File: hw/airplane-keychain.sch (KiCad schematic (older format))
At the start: 11 parts, among them IC1 ATTINY85-P, SW1 SW_PUSH, SW2 SPST

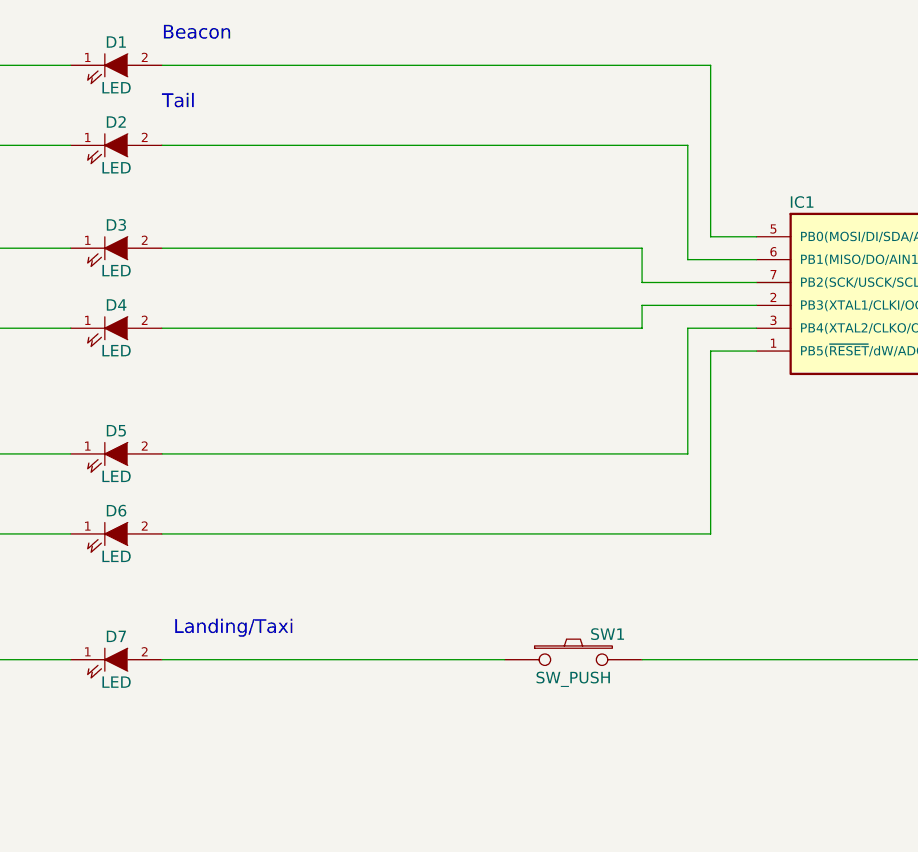
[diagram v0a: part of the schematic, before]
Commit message: added current limiting resistors
swapped out battery connector
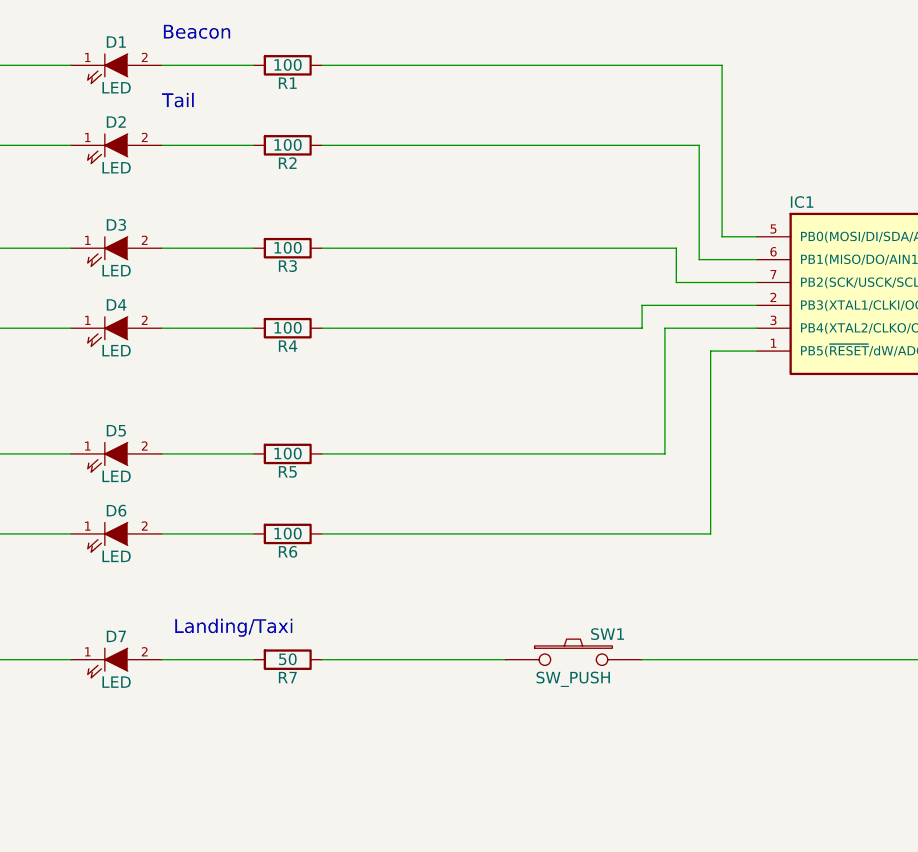
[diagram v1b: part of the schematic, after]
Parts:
- added R1, R2, R3, R4, R5, R6: 100, Resistors_ThroughHole:R_Axial_DIN0207_L6.3mm_D2.5mm_P2.54mm_Vertical, symbol R
- added R7: 50, Resistors_ThroughHole:R_Axial_DIN0207_L6.3mm_D2.5mm_P2.54mm_Vertical, symbol R
- BT1: footprint Battery_Holders:Keystone_2468_2xAAA -> Connectors_JST:JST_PH_B2B-PH-K_02x2.00mm_Straight
- SW1: footprint Buttons_Switches_ThroughHole:SW_PUSH-12mm -> Buttons_Switches_ThroughHole:SW_PUSH_SMALL
- SW2: footprint Buttons_Switches_ThroughHole:SW_DIP_x1_W7.62mm_Slide -> Buttons_Switches_ThroughHole:SW_Micro_SPST
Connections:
- net at D1.2 (A): now also R1.2; no longer IC1.5 (PB0(MOSI/DI/SDA/AIN0/OC0A/OC1A/AREF/PCINT0))
- net at D2.2 (A): now also R2.2; no longer IC1.6 (PB1(MISO/DO/AIN1/OC0B/OC1A/PCINT1))
- net at D3.2 (A): now also R3.2; no longer IC1.7 (PB2(SCK/USCK/SCL/T0/INT0/ADC1/PCINT2))
- net at D4.2 (A): now also R4.2; no longer IC1.2 (PB3(XTAL1/CLKI/OC1B/ADC3/PCINT3))
- net at D5.2 (A): now also R5.2; no longer IC1.3 (PB4(XTAL2/CLKO/OC1B/ADC2/PCINT4))
- net at D6.2 (A): now also R6.2; no longer IC1.1 (PB5(~RESET~/dW/ADC0/PCINT5))
- net at D7.2 (A): now also R7.2; no longer SW1.1
- new net: R7.1, SW1.1
- new net: IC1.1 (PB5(~RESET~/dW/ADC0/PCINT5)), R6.1
- new net: IC1.2 (PB3(XTAL1/CLKI/OC1B/ADC3/PCINT3)), R4.1
- new net: IC1.3 (PB4(XTAL2/CLKO/OC1B/ADC2/PCINT4)), R5.1
- new net: IC1.5 (PB0(MOSI/DI/SDA/AIN0/OC0A/OC1A/AREF/PCINT0)), R1.1
- new net: IC1.6 (PB1(MISO/DO/AIN1/OC0B/OC1A/PCINT1)), R2.1
- new net: IC1.7 (PB2(SCK/USCK/SCL/T0/INT0/ADC1/PCINT2)), R3.1
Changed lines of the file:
@@
 F 0 "SW1" H 3950 3860 50  0000 C CNN
 F 1 "SW_PUSH" H 3800 3670 50  0000 C CNN
-F 2 "Buttons_Switches_ThroughHole:SW_PUSH-12mm" H 3800 3750 50  0001 C CNN
+F 2 "Buttons_Switches_ThroughHole:SW_PUSH_SMALL" H 3800 3750 50  0001 C CNN
 F 3 "" H 3800 3750 50  0000 C CNN
 	1    3800 3750
@@
 F 0 "BT1" H 8400 3850 50  0000 L CNN
 F 1 "Battery" H 8400 3750 50  0000 L CNN
-F 2 "Battery_Holders:Keystone_2468_2xAAA" V 8300 3840 50  0001 C CNN
+F 2 "Connectors_JST:JST_PH_B2B-PH-K_02x2.00mm_Straight" V 8300 3840 50  0001 C CNN
 F 3 "" V 8300 3840 50  0000 C CNN
 	1    8300 3800
@@
 F 0 "SW2" H 8300 2700 50  0000 C CNN
 F 1 "SPST" H 8300 2500 50  0000 C CNN
-F 2 "Buttons_Switches_ThroughHole:SW_DIP_x1_W7.62mm_Slide" H 8300 2600 50  0001 C CNN
+F 2 "Buttons_Switches_ThroughHole:SW_Micro_SPST" H 8300 2600 50  0001 C CNN
 F 3 "" H 8300 2600 50  0000 C CNN
 	1    8300 2600
@@
 	8300 3950 8300 4150
 Wire Wire Line
-	3500 3750 2000 3750
-Wire Wire Line
 	4100 3750 7900 3750
 Wire Wire Line
@@
 	1    0    0    -1
 $EndComp
-Wire Wire Line
-	2000 1150 4400 1150
-Wire Wire Line
-	4400 1150 4400 1900
-Wire Wire Line
-	4400 1900 4600 1900
-Wire Wire Line
-	2000 1500 4300 1500
-Wire Wire Line
-	4300 1500 4300 2000
-Wire Wire Line
-	4300 2000 4600 2000
 Text Notes 2000 1050 0    60   ~ 0
 Beacon
 Text Notes 2000 1350 0    60   ~ 0
 Tail
-Wire Wire Line
-	2000 1950 4100 1950
-Wire Wire Line
-	4100 1950 4100 2100
-Wire Wire Line
-	4100 2100 4600 2100
-Wire Wire Line
-	2000 2300 4100 2300
-Wire Wire Line
-	4100 2300 4100 2200
-Wire Wire Line
-	4100 2200 4600 2200
-Wire Wire Line
-	2000 2850 4300 2850
-Wire Wire Line
-	4300 2850 4300 2300
-Wire Wire Line
-	4300 2300 4600 2300
-Wire Wire Line
-	2000 3200 4400 3200
-Wire Wire Line
-	4400 3200 4400 2400
-Wire Wire Line
-	4400 2400 4600 2400
 Text Notes 2050 3650 0    60   ~ 0
 Landing/Taxi
@@
 Wire Wire Line
 	8300 1900 8300 2100
+$Comp
+L R R1
+U 1 1 58E07A9A
+P 2550 1150
+F 0 "R1" V 2630 1150 50  0000 C CNN
+F 1 "100" V 2550 1150 50  0000 C CNN
+F 2 "Resistors_ThroughHole:R_Axial_DIN0207_L6.3mm_D2.5mm_P2.54mm_Vertical" V 2480 1150 50  0001 C CNN
+F 3 "" H 2550 1150 50  0001 C CNN
+	1    2550 1150
+	0    1    1    0
+$EndComp
+$Comp
+L R R2
+U 1 1 58E07B96
+P 2550 1500
+F 0 "R2" V 2630 1500 50  0000 C CNN
+F 1 "100" V 2550 1500 50  0000 C CNN
+F 2 "Resistors_ThroughHole:R_Axial_DIN0207_L6.3mm_D2.5mm_P2.54mm_Vertical" V 2480 1500 50  0001 C CNN
+F 3 "" H 2550 1500 50  0001 C CNN
+	1    2550 1500
+	0    1    1    0
+$EndComp
+$Comp
+L R R3
+U 1 1 58E07BFF
+P 2550 1950
+F 0 "R3" V 2630 1950 50  0000 C CNN
+F 1 "100" V 2550 1950 50  0000 C CNN
+F 2 "Resistors_ThroughHole:R_Axial_DIN0207_L6.3mm_D2.5mm_P2.54mm_Vertical" V 2480 1950 50  0001 C CNN
+F 3 "" H 2550 1950 50  0001 C CNN
+	1    2550 1950
+	0    1    1    0
+$EndComp
+$Comp
+L R R4
+U 1 1 58E07C60
+P 2550 2300
+F 0 "R4" V 2630 2300 50  0000 C CNN
+F 1 "100" V 2550 2300 50  0000 C CNN
+F 2 "Resistors_ThroughHole:R_Axial_DIN0207_L6.3mm_D2.5mm_P2.54mm_Vertical" V 2480 2300 50  0001 C CNN
+F 3 "" H 2550 2300 50  0001 C CNN
+	1    2550 2300
+	0    1    1    0
+$EndComp
+$Comp
+L R R5
+U 1 1 58E07CA3
+P 2550 2850
+F 0 "R5" V 2630 2850 50  0000 C CNN
+F 1 "100" V 2550 2850 50  0000 C CNN
+F 2 "Resistors_ThroughHole:R_Axial_DIN0207_L6.3mm_D2.5mm_P2.54mm_Vertical" V 2480 2850 50  0001 C CNN
+F 3 "" H 2550 2850 50  0001 C CNN
+	1    2550 2850
+	0    1    1    0
+$EndComp
+$Comp
+L R R6
+U 1 1 58E07CDC
+P 2550 3200
+F 0 "R6" V 2630 3200 50  0000 C CNN
+F 1 "100" V 2550 3200 50  0000 C CNN
+F 2 "Resistors_ThroughHole:R_Axial_DIN0207_L6.3mm_D2.5mm_P2.54mm_Vertical" V 2480 3200 50  0001 C CNN
+F 3 "" H 2550 3200 50  0001 C CNN
+	1    2550 3200
+	0    1    1    0
+$EndComp
+$Comp
+L R R7
+U 1 1 58E07D29
+P 2550 3750
+F 0 "R7" V 2630 3750 50  0000 C CNN
+F 1 "50" V 2550 3750 50  0000 C CNN
+F 2 "Resistors_ThroughHole:R_Axial_DIN0207_L6.3mm_D2.5mm_P2.54mm_Vertical" V 2480 3750 50  0001 C CNN
+F 3 "" H 2550 3750 50  0001 C CNN
+	1    2550 3750
+	0    1    1    0
+$EndComp
+Wire Wire Line
+	2000 1150 2400 1150
+Wire Wire Line
+	2700 1150 4450 1150
+Wire Wire Line
+	4450 1150 4450 1900
+Wire Wire Line
+	4450 1900 4600 1900
+Wire Wire Line
+	2000 1500 2400 1500
+Wire Wire Line
+	2700 1500 4350 1500
+Wire Wire Line
+	4350 1500 4350 2000
+Wire Wire Line
+	4350 2000 4600 2000
+Wire Wire Line
+	2000 1950 2400 1950
+Wire Wire Line
+	2700 1950 4250 1950
+Wire Wire Line
+	4250 1950 4250 2100
+Wire Wire Line
+	4250 2100 4600 2100
+Wire Wire Line
+	2000 2300 2400 2300
+Wire Wire Line
+	2700 2300 4100 2300
+Wire Wire Line
+	4100 2300 4100 2200
+Wire Wire Line
+	4100 2200 4600 2200
+Wire Wire Line
+	2000 2850 2400 2850
+Wire Wire Line
+	2700 2850 4200 2850
+Wire Wire Line
+	4200 2850 4200 2300
+Wire Wire Line
+	4200 2300 4600 2300
+Wire Wire Line
+	2000 3200 2400 3200
+Wire Wire Line
+	2700 3200 4400 3200
+Wire Wire Line
+	4400 3200 4400 2400
+Wire Wire Line
+	4400 2400 4600 2400
+Wire Wire Line
+	2000 3750 2400 3750
+Wire Wire Line
+	2700 3750 3500 3750
 $EndSCHEMATC

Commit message: Added second battery
Changed some footprints
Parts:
- removed BT1: Battery, Connectors_JST:JST_PH_B2B-PH-K_02x2.00mm_Straight, symbol Battery-RESCUE-airplane-keychain
- added BT1, BT2: Battery_Cell, Battery_Holders:Keystone_1058_1x2032-CoinCell, symbol Battery_Cell
- R1, R2, R3, R4, R5, R6, R7: footprint Resistors_ThroughHole:R_Axial_DIN0207_L6.3mm_D2.5mm_P2.54mm_Vertical -> Resistors_ThroughHole:R_Axial_DIN0411_L9.9mm_D3.6mm_P5.08mm_Vertical
- SW1: footprint Buttons_Switches_ThroughHole:SW_PUSH_SMALL -> Buttons_Switches_ThroughHole:SW_PUSH_6mm_h9.5mm
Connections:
- net GND: now also BT1.2 (-), BT2.2 (-)
- net at SW1.2, SW2.2: now also BT1.1 (+), BT2.1 (+)
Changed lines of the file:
@@
 F 0 "SW1" H 3950 3860 50  0000 C CNN
 F 1 "SW_PUSH" H 3800 3670 50  0000 C CNN
-F 2 "Buttons_Switches_ThroughHole:SW_PUSH_SMALL" H 3800 3750 50  0001 C CNN
+F 2 "Buttons_Switches_ThroughHole:SW_PUSH_6mm_h9.5mm" H 3800 3750 50  0001 C CNN
 F 3 "" H 3800 3750 50  0000 C CNN
 	1    3800 3750
@@
 $EndComp
 $Comp
-L Battery-RESCUE-airplane-keychain BT1
-U 1 1 58D828CF
-P 8300 3800
-F 0 "BT1" H 8400 3850 50  0000 L CNN
-F 1 "Battery" H 8400 3750 50  0000 L CNN
-F 2 "Connectors_JST:JST_PH_B2B-PH-K_02x2.00mm_Straight" V 8300 3840 50  0001 C CNN
-F 3 "" V 8300 3840 50  0000 C CNN
-	1    8300 3800
-	1    0    0    -1
-$EndComp
-$Comp
 L SPST SW2
 U 1 1 58D82980
@@
 	7900 3750 7900 3400
 Wire Wire Line
-	7900 3400 8300 3400
+	7900 3400 8850 3400
 Connection ~ 8300 3400
 Wire Wire Line
@@
 F 0 "R1" V 2630 1150 50  0000 C CNN
 F 1 "100" V 2550 1150 50  0000 C CNN
-F 2 "Resistors_ThroughHole:R_Axial_DIN0207_L6.3mm_D2.5mm_P2.54mm_Vertical" V 2480 1150 50  0001 C CNN
+F 2 "Resistors_ThroughHole:R_Axial_DIN0411_L9.9mm_D3.6mm_P5.08mm_Vertical" V 2480 1150 50  0001 C CNN
 F 3 "" H 2550 1150 50  0001 C CNN
 	1    2550 1150
@@
 F 0 "R2" V 2630 1500 50  0000 C CNN
 F 1 "100" V 2550 1500 50  0000 C CNN
-F 2 "Resistors_ThroughHole:R_Axial_DIN0207_L6.3mm_D2.5mm_P2.54mm_Vertical" V 2480 1500 50  0001 C CNN
+F 2 "Resistors_ThroughHole:R_Axial_DIN0411_L9.9mm_D3.6mm_P5.08mm_Vertical" V 2480 1500 50  0001 C CNN
 F 3 "" H 2550 1500 50  0001 C CNN
 	1    2550 1500
@@
 F 0 "R3" V 2630 1950 50  0000 C CNN
 F 1 "100" V 2550 1950 50  0000 C CNN
-F 2 "Resistors_ThroughHole:R_Axial_DIN0207_L6.3mm_D2.5mm_P2.54mm_Vertical" V 2480 1950 50  0001 C CNN
+F 2 "Resistors_ThroughHole:R_Axial_DIN0411_L9.9mm_D3.6mm_P5.08mm_Vertical" V 2480 1950 50  0001 C CNN
 F 3 "" H 2550 1950 50  0001 C CNN
 	1    2550 1950
@@
 F 0 "R4" V 2630 2300 50  0000 C CNN
 F 1 "100" V 2550 2300 50  0000 C CNN
-F 2 "Resistors_ThroughHole:R_Axial_DIN0207_L6.3mm_D2.5mm_P2.54mm_Vertical" V 2480 2300 50  0001 C CNN
+F 2 "Resistors_ThroughHole:R_Axial_DIN0411_L9.9mm_D3.6mm_P5.08mm_Vertical" V 2480 2300 50  0001 C CNN
 F 3 "" H 2550 2300 50  0001 C CNN
 	1    2550 2300
@@
 F 0 "R5" V 2630 2850 50  0000 C CNN
 F 1 "100" V 2550 2850 50  0000 C CNN
-F 2 "Resistors_ThroughHole:R_Axial_DIN0207_L6.3mm_D2.5mm_P2.54mm_Vertical" V 2480 2850 50  0001 C CNN
+F 2 "Resistors_ThroughHole:R_Axial_DIN0411_L9.9mm_D3.6mm_P5.08mm_Vertical" V 2480 2850 50  0001 C CNN
 F 3 "" H 2550 2850 50  0001 C CNN
 	1    2550 2850
@@
 F 0 "R6" V 2630 3200 50  0000 C CNN
 F 1 "100" V 2550 3200 50  0000 C CNN
-F 2 "Resistors_ThroughHole:R_Axial_DIN0207_L6.3mm_D2.5mm_P2.54mm_Vertical" V 2480 3200 50  0001 C CNN
+F 2 "Resistors_ThroughHole:R_Axial_DIN0411_L9.9mm_D3.6mm_P5.08mm_Vertical" V 2480 3200 50  0001 C CNN
 F 3 "" H 2550 3200 50  0001 C CNN
 	1    2550 3200
@@
 F 0 "R7" V 2630 3750 50  0000 C CNN
 F 1 "50" V 2550 3750 50  0000 C CNN
-F 2 "Resistors_ThroughHole:R_Axial_DIN0207_L6.3mm_D2.5mm_P2.54mm_Vertical" V 2480 3750 50  0001 C CNN
+F 2 "Resistors_ThroughHole:R_Axial_DIN0411_L9.9mm_D3.6mm_P5.08mm_Vertical" V 2480 3750 50  0001 C CNN
 F 3 "" H 2550 3750 50  0001 C CNN
 	1    2550 3750
@@
 Wire Wire Line
 	2700 3750 3500 3750
+$Comp
+L Battery_Cell BT2
+U 1 1 58E71486
+P 8850 3850
+F 0 "BT2" H 8950 3950 50  0000 L CNN
+F 1 "Battery_Cell" H 8950 3850 50  0000 L CNN
+F 2 "Battery_Holders:Keystone_1058_1x2032-CoinCell" V 8850 3910 50  0001 C CNN
+F 3 "" V 8850 3910 50  0001 C CNN
+	1    8850 3850
+	1    0    0    -1
+$EndComp
+$Comp
+L Battery_Cell BT1
+U 1 1 58E7150B
+P 8300 3850
+F 0 "BT1" H 8400 3950 50  0000 L CNN
+F 1 "Battery_Cell" H 8400 3850 50  0000 L CNN
+F 2 "Battery_Holders:Keystone_1058_1x2032-CoinCell" V 8300 3910 50  0001 C CNN
+F 3 "" V 8300 3910 50  0001 C CNN
+	1    8300 3850
+	1    0    0    -1
+$EndComp
+Wire Wire Line
+	8850 3400 8850 3650
+Wire Wire Line
+	8850 3950 8850 4050
+Wire Wire Line
+	8850 4050 8300 4050
+Connection ~ 8300 4050
 $EndSCHEMATC

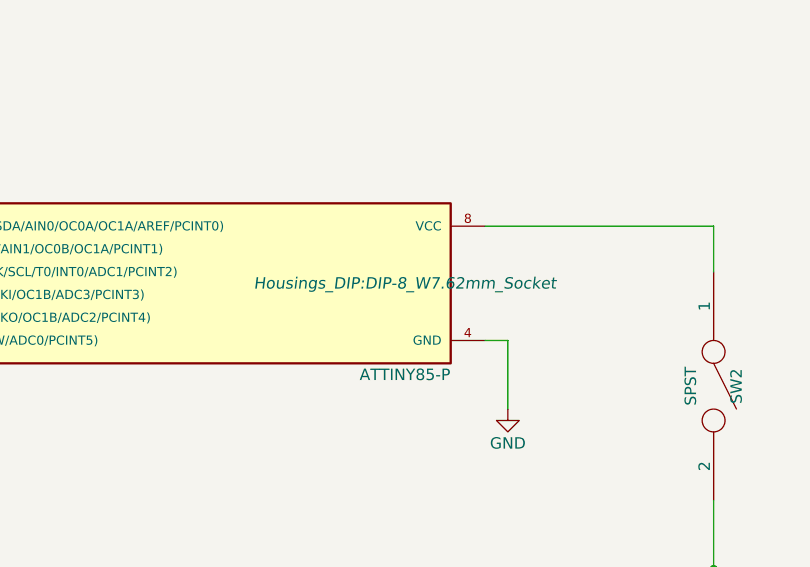
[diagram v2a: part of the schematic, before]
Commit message: Update to schematic
Minor part changes
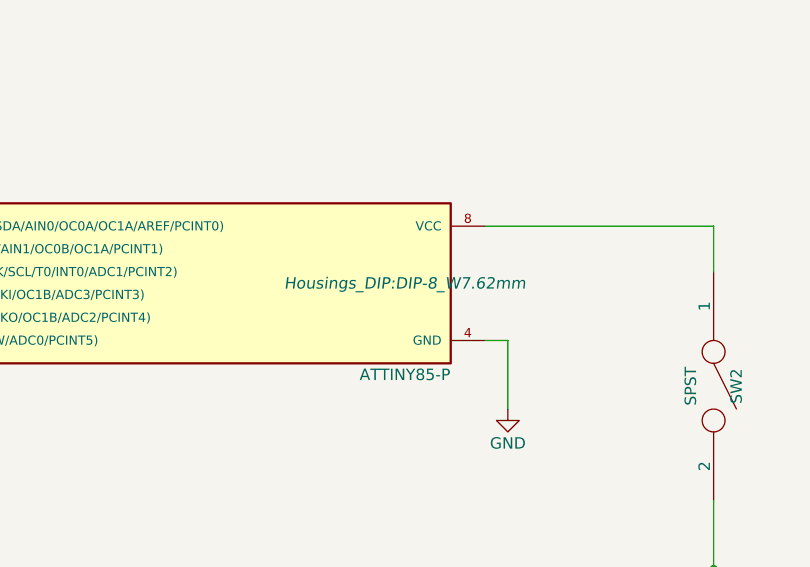
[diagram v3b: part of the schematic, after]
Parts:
- IC1: footprint Housings_DIP:DIP-8_W7.62mm_Socket -> Housings_DIP:DIP-8_W7.62mm
- R1, R2, R3, R4, R5, R6, R7: footprint Resistors_ThroughHole:R_Axial_DIN0411_L9.9mm_D3.6mm_P5.08mm_Vertical -> Resistors_THT:R_Axial_DIN0309_L9.0mm_D3.2mm_P12.70mm_Horizontal
- SW1: footprint Buttons_Switches_ThroughHole:SW_PUSH_6mm_h9.5mm -> Buttons_Switches_THT:SW_PUSH_6mm
- SW2: footprint Buttons_Switches_ThroughHole:SW_Micro_SPST -> Buttons_Switches_THT:SW_Micro_SPST
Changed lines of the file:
@@
 F 0 "SW1" H 3950 3860 50  0000 C CNN
 F 1 "SW_PUSH" H 3800 3670 50  0000 C CNN
-F 2 "Buttons_Switches_ThroughHole:SW_PUSH_6mm_h9.5mm" H 3800 3750 50  0001 C CNN
+F 2 "Buttons_Switches_THT:SW_PUSH_6mm" H 3800 3750 50  0001 C CNN
 F 3 "" H 3800 3750 50  0000 C CNN
 	1    3800 3750
@@
 F 0 "IC1" H 4800 2550 50  0000 C CNN
 F 1 "ATTINY85-P" H 6950 1750 50  0000 C CNN
-F 2 "Housings_DIP:DIP-8_W7.62mm_Socket" H 6950 2150 50  0000 C CIN
+F 2 "Housings_DIP:DIP-8_W7.62mm" H 6950 2150 50  0000 C CIN
 F 3 "" H 5950 2150 50  0000 C CNN
 	1    5950 2150
@@
 F 0 "SW2" H 8300 2700 50  0000 C CNN
 F 1 "SPST" H 8300 2500 50  0000 C CNN
-F 2 "Buttons_Switches_ThroughHole:SW_Micro_SPST" H 8300 2600 50  0001 C CNN
+F 2 "Buttons_Switches_THT:SW_Micro_SPST" H 8300 2600 50  0001 C CNN
 F 3 "" H 8300 2600 50  0000 C CNN
 	1    8300 2600
@@
 F 0 "R1" V 2630 1150 50  0000 C CNN
 F 1 "100" V 2550 1150 50  0000 C CNN
-F 2 "Resistors_ThroughHole:R_Axial_DIN0411_L9.9mm_D3.6mm_P5.08mm_Vertical" V 2480 1150 50  0001 C CNN
+F 2 "Resistors_THT:R_Axial_DIN0309_L9.0mm_D3.2mm_P12.70mm_Horizontal" V 2480 1150 50  0001 C CNN
 F 3 "" H 2550 1150 50  0001 C CNN
 	1    2550 1150
@@
 F 0 "R2" V 2630 1500 50  0000 C CNN
 F 1 "100" V 2550 1500 50  0000 C CNN
-F 2 "Resistors_ThroughHole:R_Axial_DIN0411_L9.9mm_D3.6mm_P5.08mm_Vertical" V 2480 1500 50  0001 C CNN
+F 2 "Resistors_THT:R_Axial_DIN0309_L9.0mm_D3.2mm_P12.70mm_Horizontal" V 2480 1500 50  0001 C CNN
 F 3 "" H 2550 1500 50  0001 C CNN
 	1    2550 1500
@@
 F 0 "R3" V 2630 1950 50  0000 C CNN
 F 1 "100" V 2550 1950 50  0000 C CNN
-F 2 "Resistors_ThroughHole:R_Axial_DIN0411_L9.9mm_D3.6mm_P5.08mm_Vertical" V 2480 1950 50  0001 C CNN
+F 2 "Resistors_THT:R_Axial_DIN0309_L9.0mm_D3.2mm_P12.70mm_Horizontal" V 2480 1950 50  0001 C CNN
 F 3 "" H 2550 1950 50  0001 C CNN
 	1    2550 1950
@@
 F 0 "R4" V 2630 2300 50  0000 C CNN
 F 1 "100" V 2550 2300 50  0000 C CNN
-F 2 "Resistors_ThroughHole:R_Axial_DIN0411_L9.9mm_D3.6mm_P5.08mm_Vertical" V 2480 2300 50  0001 C CNN
+F 2 "Resistors_THT:R_Axial_DIN0309_L9.0mm_D3.2mm_P12.70mm_Horizontal" V 2480 2300 50  0001 C CNN
 F 3 "" H 2550 2300 50  0001 C CNN
 	1    2550 2300
@@
 F 0 "R5" V 2630 2850 50  0000 C CNN
 F 1 "100" V 2550 2850 50  0000 C CNN
-F 2 "Resistors_ThroughHole:R_Axial_DIN0411_L9.9mm_D3.6mm_P5.08mm_Vertical" V 2480 2850 50  0001 C CNN
+F 2 "Resistors_THT:R_Axial_DIN0309_L9.0mm_D3.2mm_P12.70mm_Horizontal" V 2480 2850 50  0001 C CNN
 F 3 "" H 2550 2850 50  0001 C CNN
 	1    2550 2850
@@
 F 0 "R6" V 2630 3200 50  0000 C CNN
 F 1 "100" V 2550 3200 50  0000 C CNN
-F 2 "Resistors_ThroughHole:R_Axial_DIN0411_L9.9mm_D3.6mm_P5.08mm_Vertical" V 2480 3200 50  0001 C CNN
+F 2 "Resistors_THT:R_Axial_DIN0309_L9.0mm_D3.2mm_P12.70mm_Horizontal" V 2480 3200 50  0001 C CNN
 F 3 "" H 2550 3200 50  0001 C CNN
 	1    2550 3200
@@
 F 0 "R7" V 2630 3750 50  0000 C CNN
 F 1 "50" V 2550 3750 50  0000 C CNN
-F 2 "Resistors_ThroughHole:R_Axial_DIN0411_L9.9mm_D3.6mm_P5.08mm_Vertical" V 2480 3750 50  0001 C CNN
+F 2 "Resistors_THT:R_Axial_DIN0309_L9.0mm_D3.2mm_P12.70mm_Horizontal" V 2480 3750 50  0001 C CNN
 F 3 "" H 2550 3750 50  0001 C CNN
 	1    2550 3750

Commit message: Final for RevA
Final changes based on prototype testing for Rev A.
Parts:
- removed R5: 100, Resistors_THT:R_Axial_DIN0309_L9.0mm_D3.2mm_P12.70mm_Horizontal, symbol R
- added J1: CONN_01X03_MALE, Pin_Headers:Pin_Header_Straight_1x03_Pitch2.54mm, symbol CONN_01X03_MALE
- D3, D4: footprint LEDs:LED_D3.0mm -> LEDs:LED_D3.0mm_Horizontal_O1.27mm_Z2.0mm
- D7: footprint LEDs:LED_D5.0mm -> LEDs:LED_D5.0mm_Horizontal_O1.27mm_Z3.0mm
- R6: value 100 -> 10k
- renumbered R7 to R5
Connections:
- net GND: now also J1.2
- net at D1.2 (A), R1.2: now also J1.3
- net at D2.2 (A), R2.2: now also J1.1
- net at D5.2 (A): now also D6.2 (A), IC1.3 (PB4(XTAL2/CLKO/OC1B/ADC2/PCINT4))
- net at R6.2: now also IC1.1 (PB5(~RESET~/dW/ADC0/PCINT5)); no longer D6.2 (A)
- net at R6.1: now also IC1.8 (VCC), SW2.1; no longer IC1.1 (PB5(~RESET~/dW/ADC0/PCINT5))
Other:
- note added: "Optional Tail Header"
- note added: "Strobe Lights"
- moved on the sheet: BT1, BT2, D1, D2, D3, D4, D5, D6, D7, IC1, R1, R2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
